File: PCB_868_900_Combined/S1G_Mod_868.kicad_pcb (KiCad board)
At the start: 4 copper layers, 50 x 40 mm, 80 parts, among them J1 S2B-PH-K-S(LF)(SN), J2 20021121-00010C4LF, J3 B4B-PH-K-S(LF)(SN), J5 0475890001-MicroUSBPort, P1 CONN_02X03, Q1 DMG2307L-7, SW1 CUS-12TB, SW2 B3U-1000P, T1 0732511150, T2 0732511150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

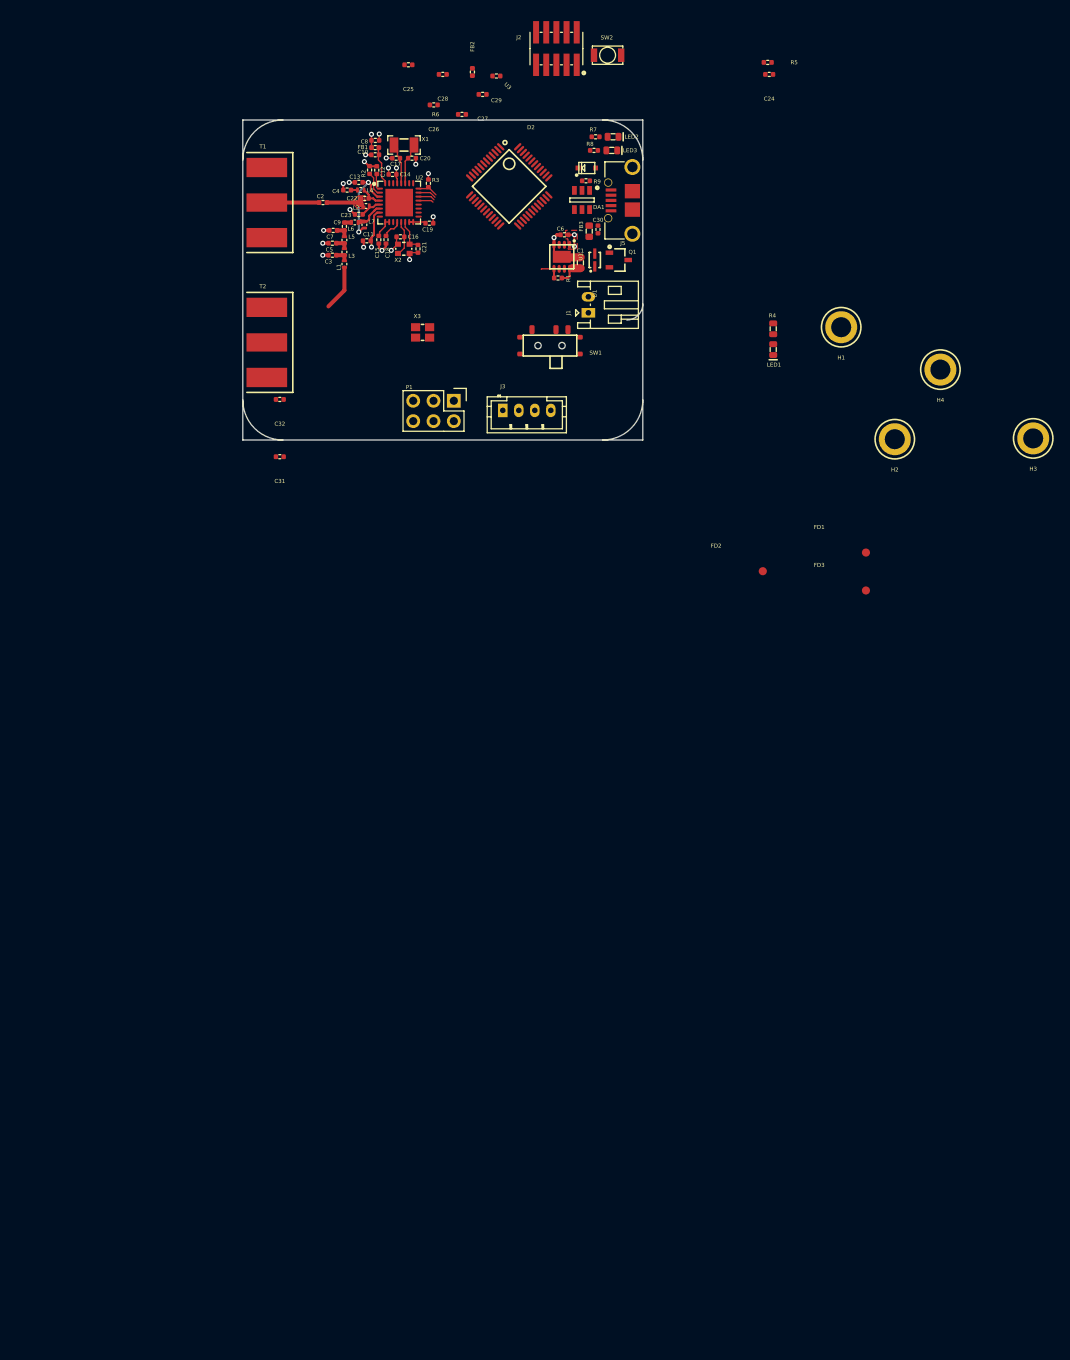
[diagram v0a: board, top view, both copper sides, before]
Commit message: Change and Progress
connecotrs change to SMA, implemented combined PA/LNA match, currently
working on that version as primary. PCB components are placed and board
size is almost set.
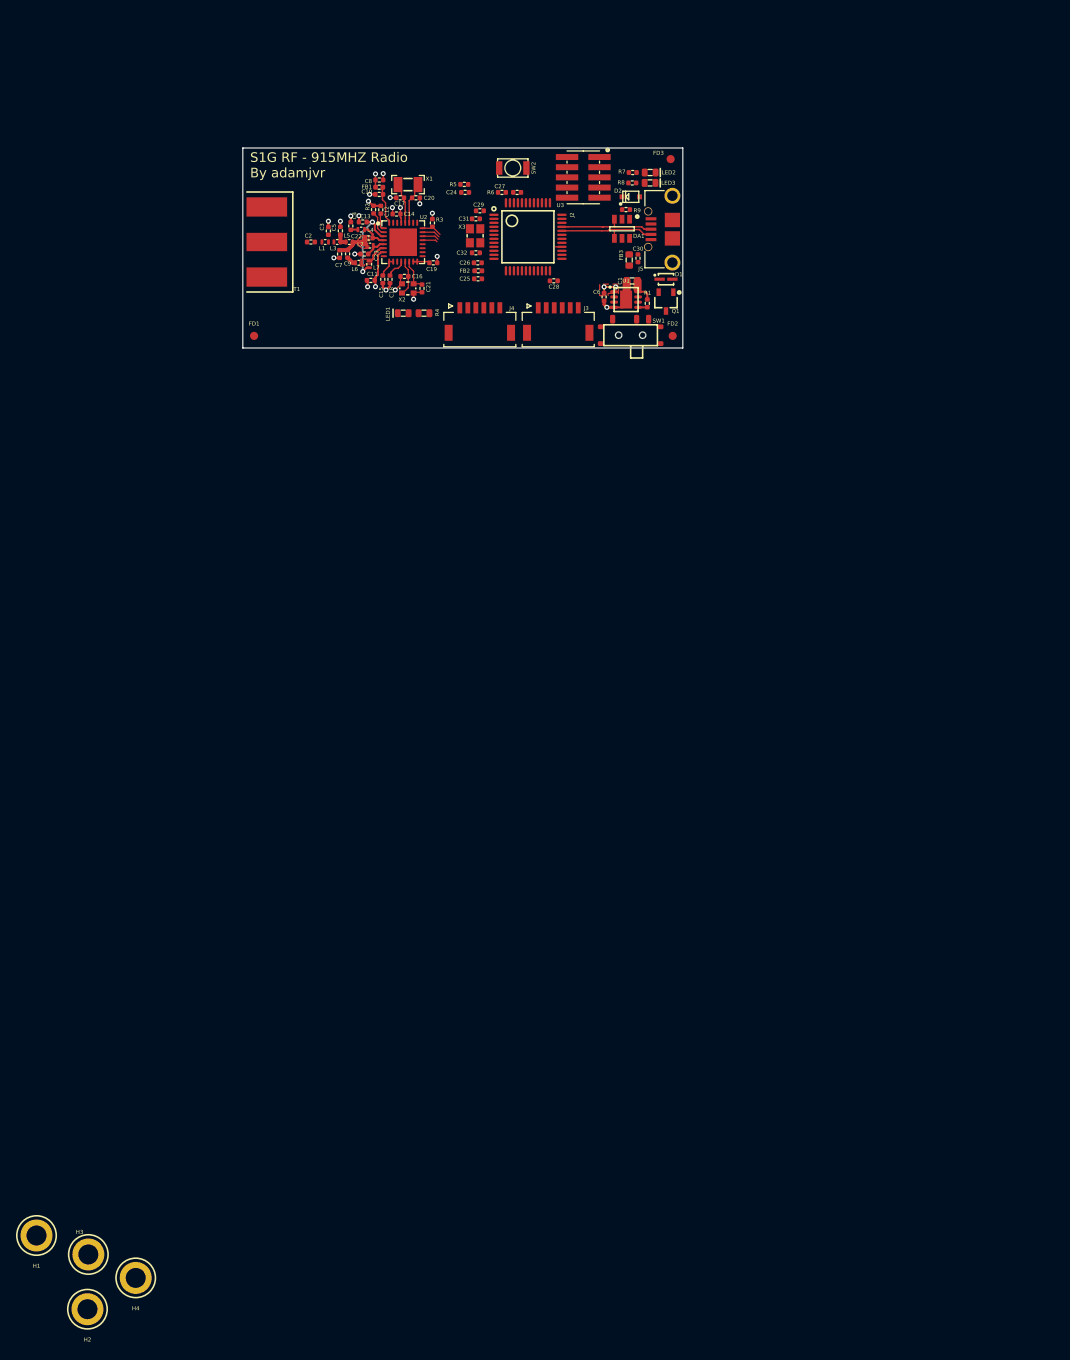
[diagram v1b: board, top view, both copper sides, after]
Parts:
- removed J1: S2B-PH-K-S(LF)(SN), PCB_Footprints:S2B-PH-K-S(LF)(SN)
- removed P1: CONN_02X03, Pin_Headers:Pin_Header_Straight_2x03
- removed T2: 0732511150, PCB_Footprints:0732511150
- added J4: SM06B-SRSS-TB(LF)(SN), PCB_Footprints:SM06B-SRSS-TB(LF)(SN), F.Cu at (86.1, 60.5)
- J3: value B4B-PH-K-S(LF)(SN) -> SM06B-SRSS-TB(LF)(SN); footprint PCB_Footprints:B4B-PH-K-S(LF)(SN) -> PCB_Footprints:SM06B-SRSS-TB(LF)(SN)
- moved H3 156.1 mm to (37.2, 177.3)
- moved H1 151.7 mm to (30.7, 174.9)
- moved H4 151.7 mm to (43.1, 180.2)
- moved H2 148.4 mm to (37.1, 184.2)
- moved FD1 81.1 mm to (57.9, 62.5)
- moved FD3 59.2 mm to (110.0, 40.4)
- moved LED1 46.5 mm to (76.5, 59.6), turned to 180 degrees
- moved R4 43.7 mm to (79.2, 59.6), turned to 180 degrees
- moved R5 40.9 mm to (84.2, 43.5)
- moved C24 40.8 mm to (84.3, 44.5)
- moved C31 38.5 mm to (85.6, 47.9)
- moved FD2 31.5 mm to (110.2, 62.5)
- moved C32 30.6 mm to (85.6, 52.1), turned to 180 degrees
- moved C28 29.3 mm to (95.4, 55.6)
- moved C25 28.1 mm to (85.9, 55.4)
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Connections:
- C22 pad 1: Net-(C2-Pad2) -> Net-(C22-Pad1)
- C7 pad 1: Net-(C7-Pad1) -> Net-(C22-Pad1)
- C9 pad 1: Net-(C7-Pad1) -> Net-(C9-Pad1)
- C9 pad 2: Net-(C9-Pad2) -> Net-(C22-Pad1)
- J3 pad 4: GND -> Net-(J3-Pad4)
- L1 pad 1: Net-(L1-Pad1) -> Net-(C2-Pad2)
- L2 pad 1: Net-(C2-Pad2) -> Net-(C22-Pad1)
- L5 pad 2: Net-(C7-Pad1) -> Net-(C22-Pad1)
- L6 pad 1: Net-(C9-Pad2) -> Net-(C9-Pad1)
- L7 pad 1: Net-(C13-Pad2) -> Net-(L6-Pad2)
- L7 pad 2: Net-(L6-Pad2) -> Net-(C13-Pad2)
- U3 pad 14: /SPI_CS -> /MCU - STM32L052K8T6/SPI2_NSS
- U3 pad 15: /SPI_SCLK -> /MCU - STM32L052K8T6/SPI2_SCLK
- U3 pad 16: /SPI_MISO -> /MCU - STM32L052K8T6/SPI2_MISO
- U3 pad 17: /SPI_MOSI -> /MCU - STM32L052K8T6/SPI2_MOSI
- U3 pad 25: /MCU - STM32L052K8T6/SPI2_NSS -> /SPI_CS
- U3 pad 26: /MCU - STM32L052K8T6/SPI2_SCLK -> /SPI_SCLK
- U3 pad 27: /MCU - STM32L052K8T6/SPI2_MISO -> /SPI_MISO
- U3 pad 28: /MCU - STM32L052K8T6/SPI2_MOSI -> /SPI_MOSI
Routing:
- net /MCU - STM32L052K8T6/USB_DM: track 0.00 -> 12.6 mm
- net /MCU - STM32L052K8T6/USB_DP: track 0.00 -> 12.4 mm
- net Net-(L1-Pad1): track 5.71 -> 0.00 mm
- net Net-(C2-Pad2): track 5.03 -> 0.00 mm
- net Net-(C2-Pad1): track 4.41 -> 0.00 mm
- net Net-(C22-Pad1): track 0.00 -> 4.38 mm
- net Net-(C7-Pad1): track 1.64 -> 0.00 mm
- net /ON_OFF: track 2.78 -> 1.16 mm
- net Net-(C3-Pad1): track 1.61 -> 0.00 mm
- net Net-(C9-Pad1): track 0.00 -> 1.16 mm
- net Net-(L6-Pad2): track 3.49 -> 2.53 mm
- net Net-(C9-Pad2): track 0.81 -> 0.00 mm
- net /SPI_MOSI: track 2.30 -> 3.07 mm
- added copper zone on F.Cu, net Net-(L6-Pad2)
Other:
- board size 50 x 40 mm -> 55 x 25 mm
- board text added: "S1G RF - 915MHZ Radio By adamjvr"

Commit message: RF Shield and more progress
Adding an RF shield to the combined implementation of the 915MHZ version
of S1G. Also experimenting with differnt connectors and what not.
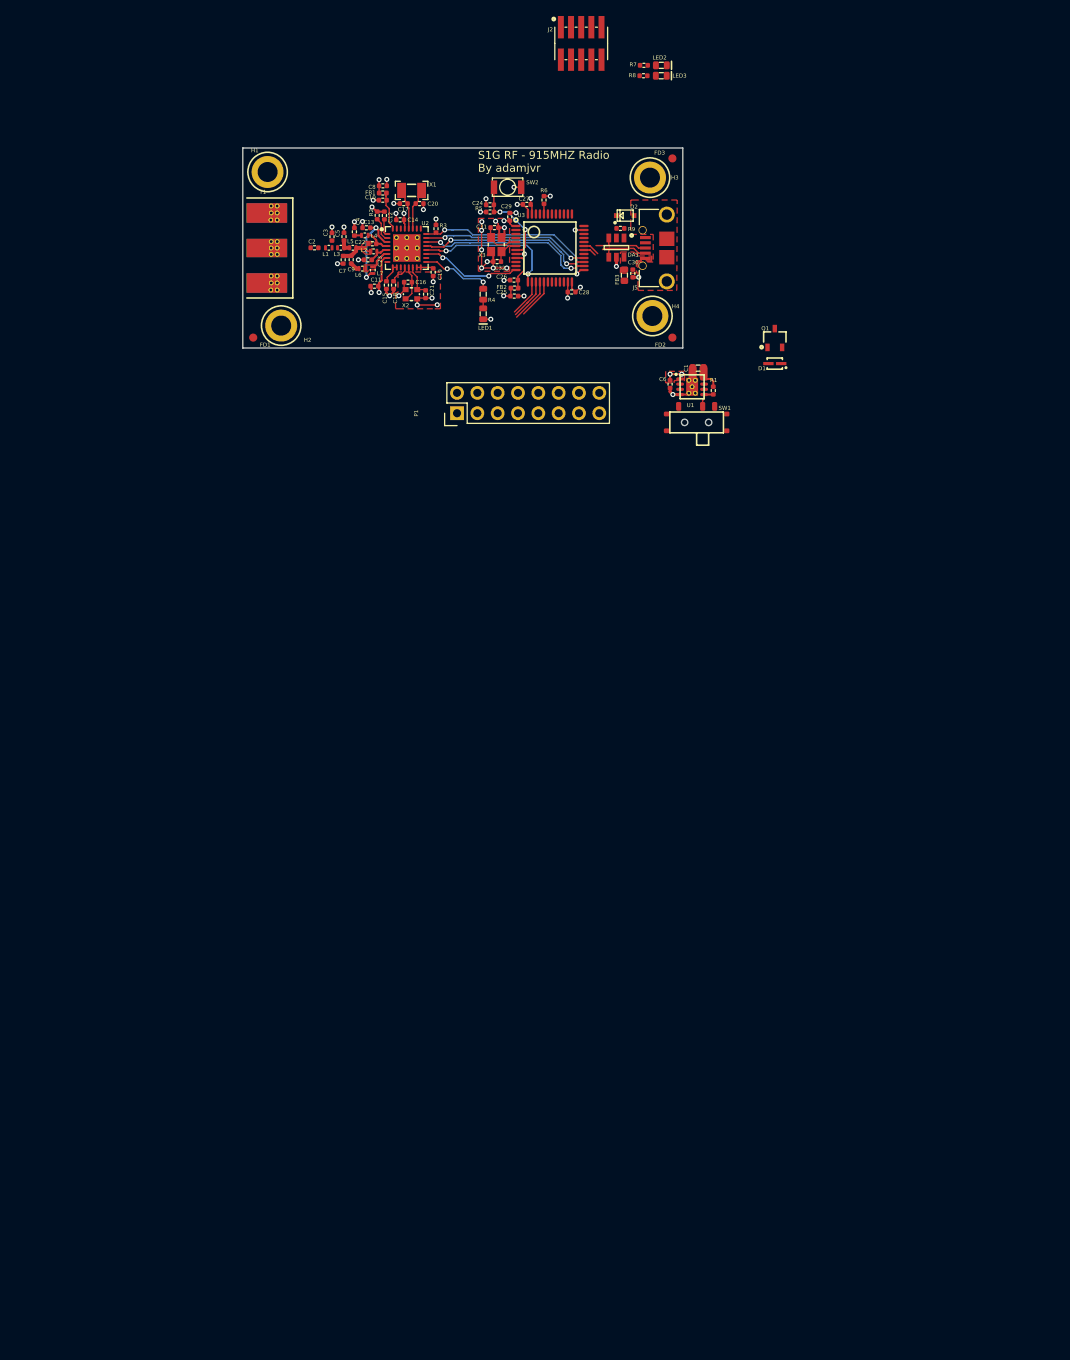
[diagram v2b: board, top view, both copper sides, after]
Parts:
- removed J3, J4: SM06B-SRSS-TB(LF)(SN), PCB_Footprints:SM06B-SRSS-TB(LF)(SN)
- added P1: CONN_02X08, Pin_Headers:Pin_Header_Straight_2x08, F.Cu at (83.3, 72.2)
- moved H3 151.8 mm to (107.4, 42.7)
- moved H4 136.5 mm to (107.7, 60.0)
- moved H1 136.0 mm to (59.6, 42.0)
- moved H2 125.3 mm to (61.3, 61.2)
- moved D1 17.2 mm to (123.0, 66.0), turned to 180 degrees
- moved J2 16.7 mm to (98.8, 25.9), turned to 180 degrees
- moved Q1 14.3 mm to (123.0, 62.8), turned to 90 degrees
- moved C1 13.7 mm to (113.4, 66.5)
- moved C6 13.7 mm to (109.9, 68.5)
- moved R1 13.7 mm to (115.3, 69.3)
- moved SW1 13.7 mm to (113.2, 73.3)
- moved U1 13.7 mm to (112.7, 68.8)
- moved LED2 13.5 mm to (108.8, 28.7)
- moved R7 13.5 mm to (106.6, 28.7)
- moved LED3 13.5 mm to (108.8, 30.0)
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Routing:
- net GND: track 24.9 -> 60.1 mm, vias 18 -> 42
- net /SPI_CS: track 2.65 -> 23.9 mm, vias 0 -> 2
- net /SPI_SCLK: track 2.09 -> 22.2 mm, vias 0 -> 2
- net /SPI_MISO: track 1.88 -> 22.0 mm, vias 0 -> 2
- net /SPI_MOSI: track 3.07 -> 21.2 mm, vias 0 -> 2
- net /MCU_IRQ: track 0.00 -> 18.0 mm, vias 0 -> 2
- net /GPIO2: track 0.00 -> 12.8 mm, vias 0 -> 2
- net /MCU - STM32L052K8T6/NRST: track 0.00 -> 11.4 mm, vias 0 -> 2
- net +3V3: track 11.5 -> 20.6 mm, vias 6 -> 11
- net Net-(R4-Pad1): track 0.00 -> 9.01 mm, vias 0 -> 2
- net /MCU - STM32L052K8T6/USB_DM: track 12.6 -> 6.79 mm
- net /MCU - STM32L052K8T6/SPI2_MISO: track 0.00 -> 5.61 mm
- net Net-(C31-Pad1): track 0.00 -> 5.57 mm
- net /MCU - STM32L052K8T6/SPI2_SCLK: track 0.00 -> 5.23 mm
- net /MCU - STM32L052K8T6/USB_DP: track 12.4 -> 7.27 mm
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- added copper zone on F.Cu, net GND
- added copper zone on F.Cu, net Net-(C22-Pad1)
- added copper zone on F.Cu, net Net-(C30-Pad2)
- added copper zone on F.Cu, net Net-(D2-Pad1)
- removed copper zone on F.Cu, net Net-(C2-Pad2)

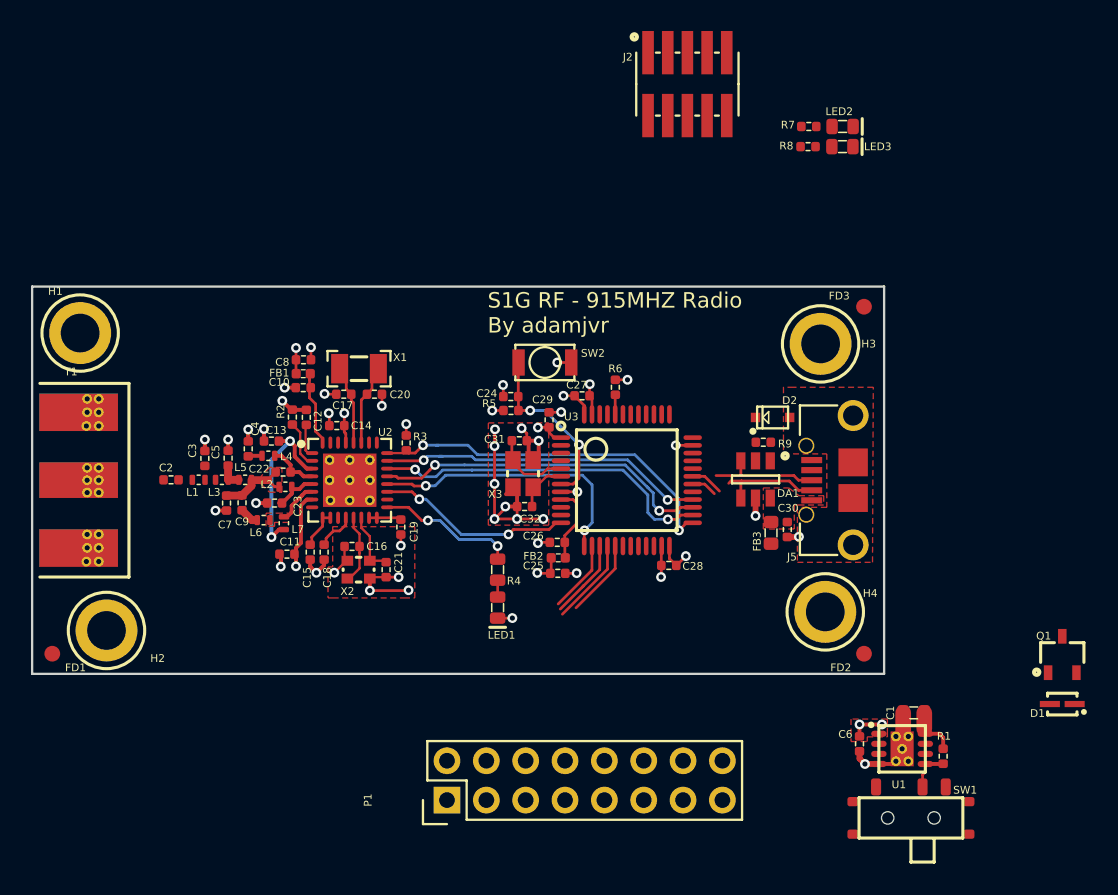
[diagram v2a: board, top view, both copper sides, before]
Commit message: First pass on PCB
First pass on PCB completed. PCB_868_900_Combined is the folder for the
finished rev.
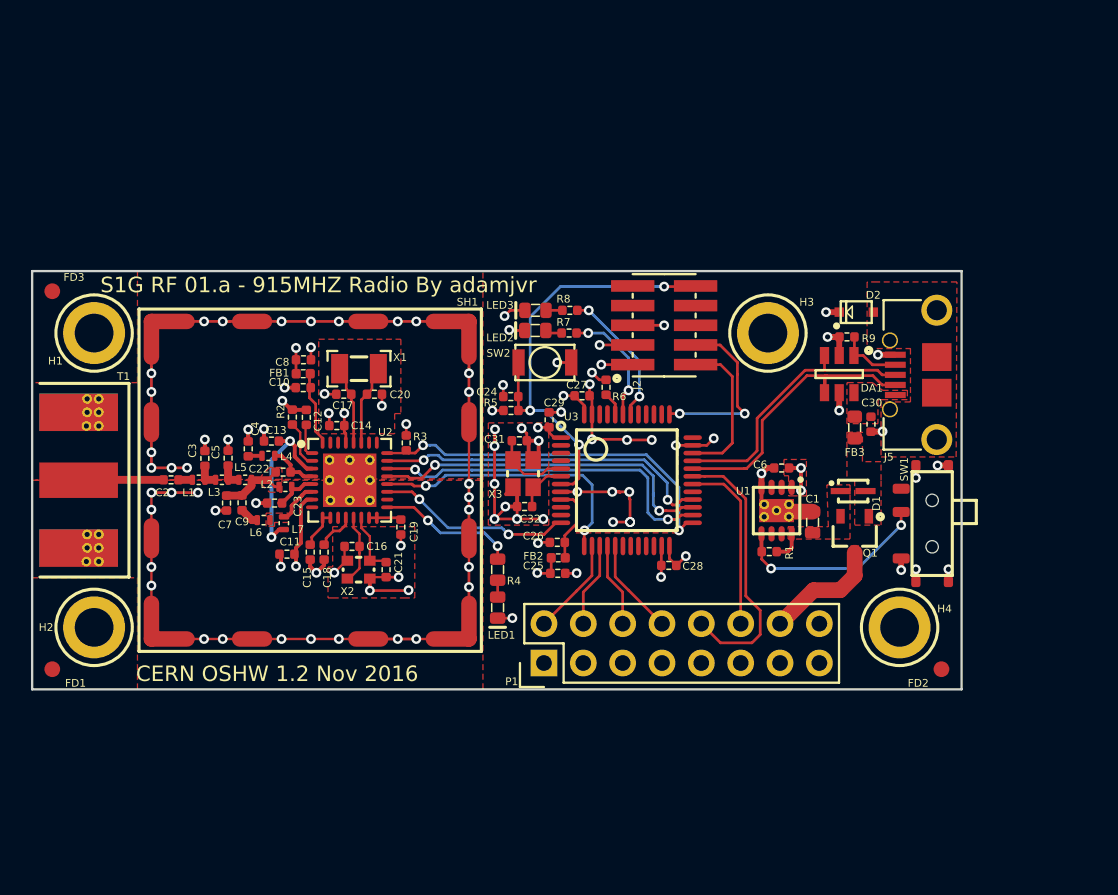
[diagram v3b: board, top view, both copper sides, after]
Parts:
- added SH1: 36103205, PCB_Footprints:36103205, F.Cu at (74.5, 51.5)
- moved FD3 52.4 mm to (57.8, 39.3)
- moved LED2 23.8 mm to (89.0, 41.8), turned to 180 degrees
- moved LED3 22.5 mm to (89.0, 40.5), turned to 180 degrees
- moved R7 20.4 mm to (91.2, 42.0), turned to 0 degrees
- moved D1 19.3 mm to (109.5, 52.2), turned to 0 degrees
- moved SW1 19.0 mm to (114.6, 54.3), turned to 90 degrees
- moved R8 18.7 mm to (91.2, 40.5), turned to 0 degrees
- moved C6 18.5 mm to (104.9, 50.7), turned to 180 degrees
- moved U1 17.4 mm to (104.6, 53.5), turned to 270 degrees
- moved R1 17.3 mm to (104.1, 56.1), turned to 0 degrees
- moved J2 15.6 mm to (97.3, 41.5), turned to 270 degrees
- moved Q1 15.5 mm to (109.6, 55.0), turned to 270 degrees
- moved C1 13.9 mm to (106.9, 54.2), turned to 90 degrees
- moved P1 10.8 mm to (89.5, 63.3)
- moved D2 8.68 mm to (109.7, 40.6)
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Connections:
- U3 pad 18: Net-(R8-Pad2) -> Net-(U3-Pad18)
- U3 pad 19: Net-(R7-Pad2) -> Net-(U3-Pad19)
- U3 pad 42: Net-(U3-Pad42) -> Net-(R8-Pad2)
- U3 pad 43: Net-(U3-Pad43) -> Net-(R7-Pad2)
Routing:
- net GND: track 60.1 -> 165.3 mm, vias 42 -> 96
- net /MCU - STM32L052K8T6/NRST: track 11.4 -> 29.0 mm, vias 2 -> 3
- net /MCU - STM32L052K8T6/USART1_RX: track 2.12 -> 17.7 mm
- net /MCU - STM32L052K8T6/SWCLK: track 0.00 -> 12.6 mm, vias 0 -> 2
- net /MCU - STM32L052K8T6/USB_DM: track 6.79 -> 19.3 mm
- net /MCU - STM32L052K8T6/SWDIO: track 0.00 -> 10.9 mm
- net /MCU - STM32L052K8T6/USB_DP: track 7.27 -> 17.8 mm
- net /ON_OFF: track 2.71 -> 12.9 mm, vias 0 -> 2
- net /MCU - STM32L052K8T6/USART1_TX: track 1.66 -> 11.5 mm
- net Net-(R8-Pad2): track 0.00 -> 9.04 mm, vias 0 -> 2
- net Net-(R7-Pad2): track 0.00 -> 7.82 mm, vias 0 -> 2
- net /PSU_IN: track 0.00 -> 7.59 mm
- net Net-(C2-Pad1): track 0.00 -> 5.49 mm
- net Net-(DA1-Pad1): track 0.00 -> 4.14 mm
- net +3V3: track 20.6 -> 22.6 mm, vias 11 -> 12
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- added copper zone on F.Cu, net /VBUS
- added copper zone on F.Cu, net /VIN
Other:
- board size 55 x 25 mm -> 60 x 27 mm
- board text added: "CERN OSHW 1.2 Nov 2016"
- board text added: "S1G RF 01.a - 915MHZ Radio By adamjvr"
- board text removed: "S1G RF - 915MHZ Radio By adamjvr"
